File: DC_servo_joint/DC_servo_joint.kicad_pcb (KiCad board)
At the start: 2 copper layers, 58.5 x 50 mm, 52 parts, among them U1 AS5600, U2 ESP32-C3-WROOM-02, U3 SP3485EN, U5 TPS563200

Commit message: Add personal Mark to the silkscreen
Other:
- board text added: "Ca(OH)2"
- board text added: "LimeRobotLab"
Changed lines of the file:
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@@
 		)
 		(property "Value" "ESP32-C3-WROOM-02"
-			(at 0 -7.975 270)
+			(at -0.55 4.225 270)
 			(layer "B.SilkS")
 			(effects
@@
 		)
 	)
+	(gr_text "Ca(OH)2"
+		(at 137.125 83.625 270)
+		(layer "B.SilkS")
+		(effects
+			(font
+				(size 2.5 2.5)
+				(thickness 0.35)
+				(italic yes)
+			)
+			(justify left bottom mirror)
+		)
+	)
 	(gr_text "GND"
 		(at 134.375 93.95 -0)
@@
 			)
 			(justify left bottom mirror)
+		)
+	)
+	(gr_text "LimeRobotLab"
+		(at 133.875 83.225 270)
+		(layer "B.SilkS")
+		(effects
+			(font
+				(size 1.5 1.5)
+				(thickness 0.2)
+				(italic yes)
+			)
+			(justify left bottom mirror)

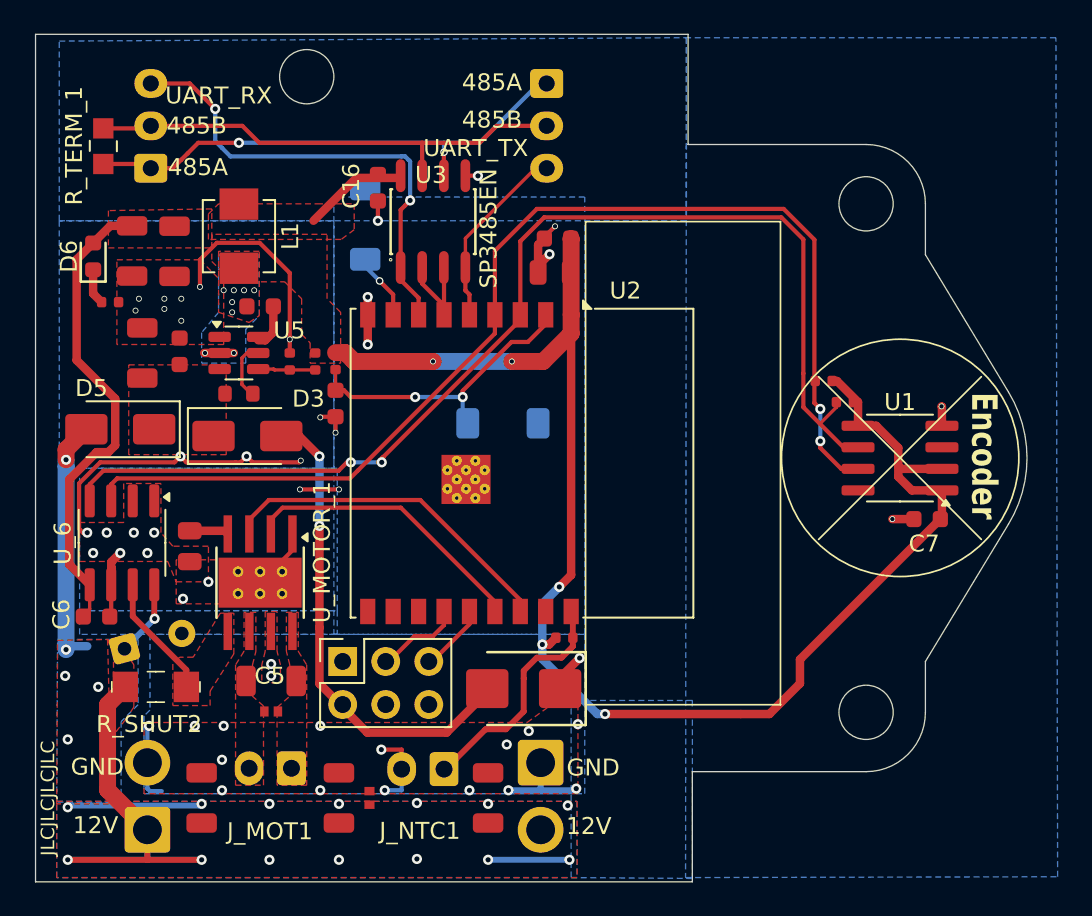
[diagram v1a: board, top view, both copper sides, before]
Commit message: Fixed the via size issue. Replace the INA219 with proper part
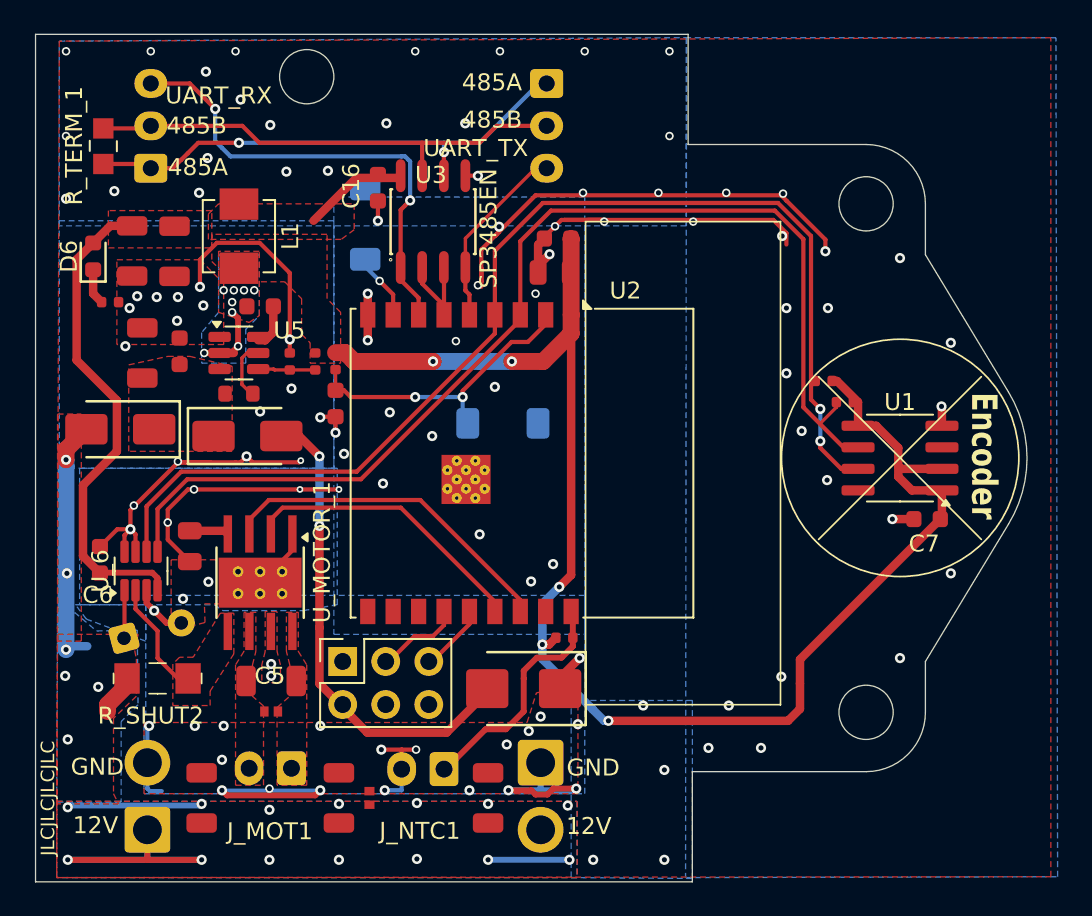
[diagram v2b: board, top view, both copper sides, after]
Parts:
- D3, D5: footprint Diode_SMD:D_SMA -> PCM_JLCPCB:D_SMA
- U_6: footprint Package_SO:SOIC-8_3.9x4.9mm_P1.27mm -> Package_TO_SOT_SMD:SOT-23-8
- moved C6 3.36 mm to (102.8, 81.0), turned to 90 degrees
- moved U_6 2.01 mm to (105.2, 81.7), turned to 90 degrees
- moved C15 0.62 mm to (104.2, 85.6)
- moved R_SHUT2 0.51 mm to (106.2, 88.0)
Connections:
- U_6 pad 1: GND -> +12V
- U_6 pad 2: GND -> /V_motor
- U_6 pad 3: /SDA -> GND
- U_6 pad 4: /SCL -> +3.3V
- U_6 pad 5: +3.3V -> /SCL
- U_6 pad 6: GND -> /SDA
- U_6 pad 7: /V_motor -> GND
- U_6 pad 8: +12V -> GND
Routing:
- net GND: track 70.3 -> 144.9 mm, vias 50 -> 111
- net +12V: track 61.3 -> 51.6 mm
- net /TPS_SW: track 1.75 -> 5.15 mm
- net /SCL: track 68.9 -> 66.8 mm, vias 2 -> 0
- net +3.3V: track 122.6 -> 124.5 mm
- net /pwm2_io3: track 17.2 -> 15.8 mm
- net /V_motor: track 7.34 -> 6.24 mm
- net /pwm1_io2: track 20.4 -> 19.6 mm

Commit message: Updated the proper value for INA219AxD and did part selection on JLC plugin
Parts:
- U_6: value INA219BxD -> INA219AxDCN
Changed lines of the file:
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@@
 			)
 		)
-		(property "Value" "INA219BxD"
+		(property "Value" "INA219AxDCN"
 			(at 0 2.4 90)
 			(layer "F.Fab")
@@
 			)
 		)
+		(property "LCSC" "C87469"
+			(at 0 0 0)
+			(layer "F.SilkS")
+			(hide yes)
+			(effects
+				(font
+					(size 1.27 1.27)
+					(thickness 0.15)
+				)
+			)
+		)
 		(property ki_fp_filters "SOT?23*")
 		(sheetname "/")
@@
 			(hide yes)
 			(effects
+				(font
+					(size 1.27 1.27)
+					(thickness 0.15)
+				)
+			)
+		)
+		(property "LCSC" "C97253"
+			(at 0 0 0)
+			(layer "F.SilkS")
+			(hide yes)
+			(effects

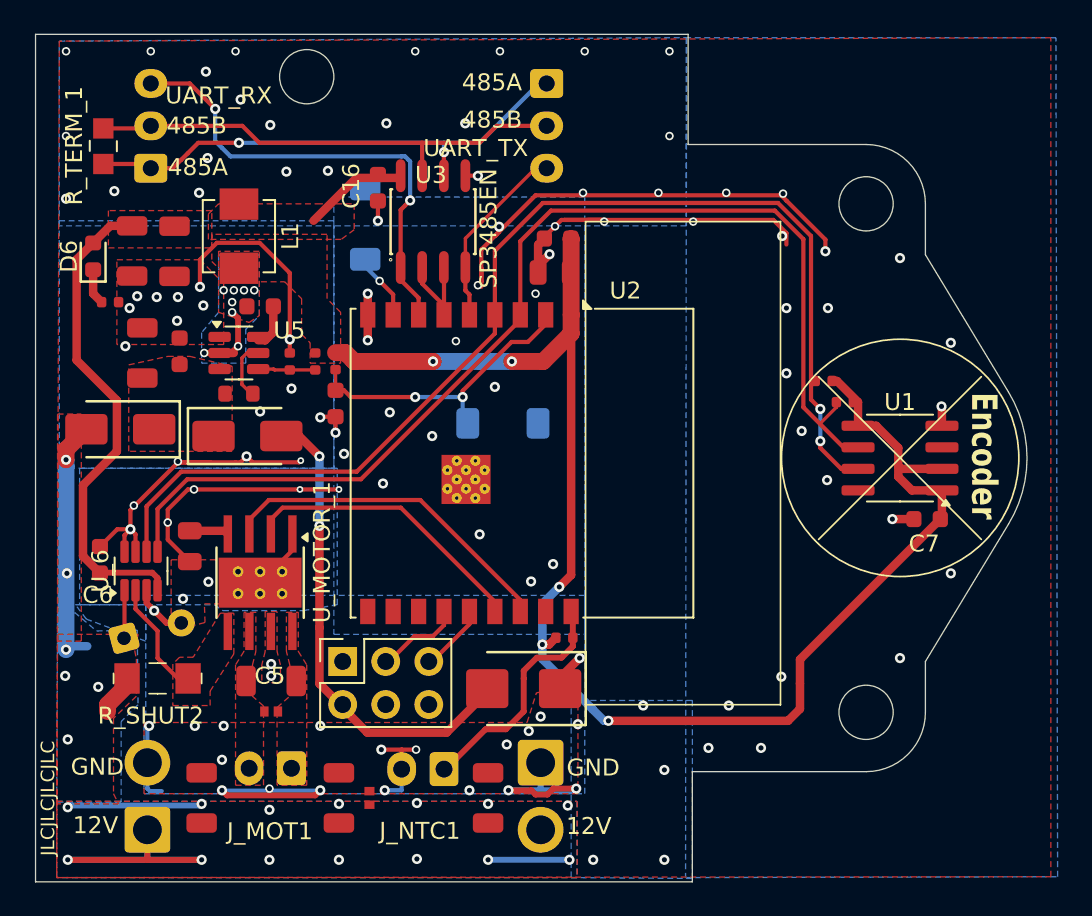
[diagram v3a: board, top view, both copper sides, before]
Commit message: Generated first trial of production file. Also added 2 rotations to parts.
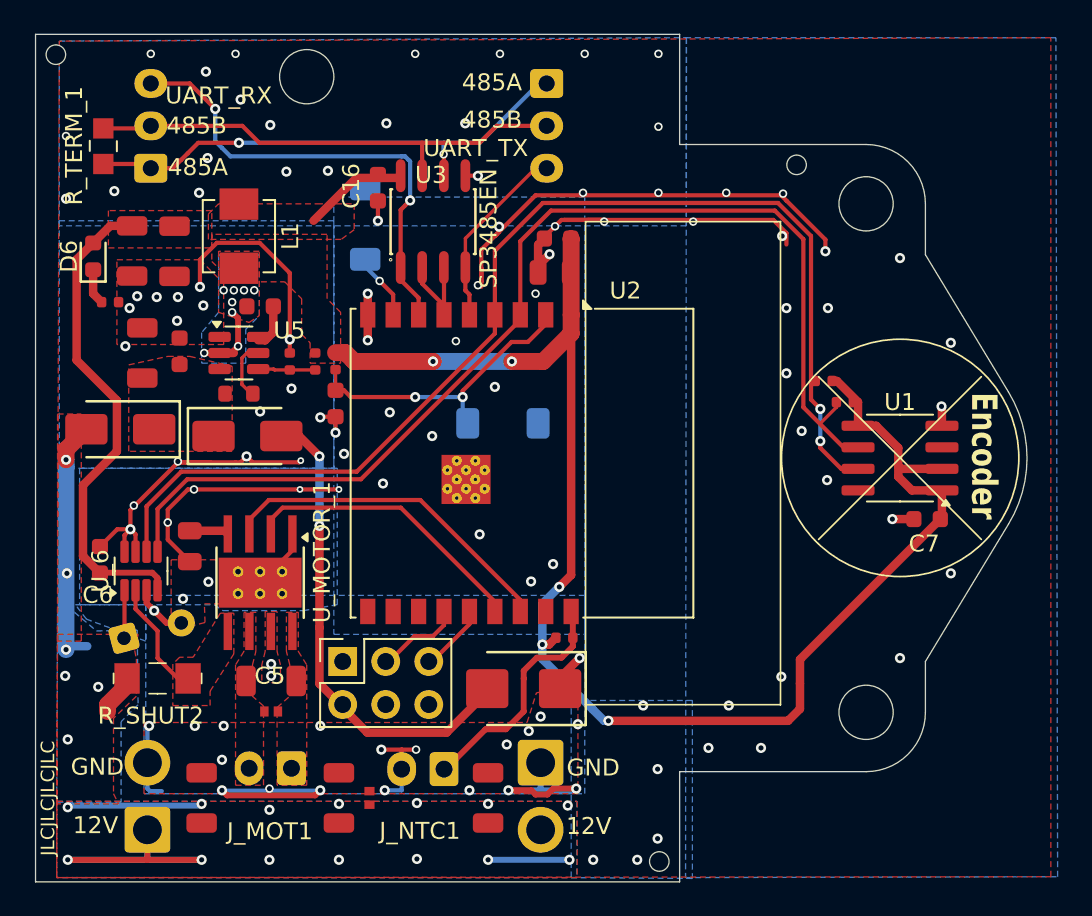
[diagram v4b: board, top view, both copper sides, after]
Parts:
- added H4: ~, PCM_JLCPCB:Hole_Tooling_JLCPCB, F.Cu at (143.9, 57.7)
- added H5: ~, PCM_JLCPCB:Hole_Tooling_JLCPCB, F.Cu at (100.2, 51.2)
- added H6: ~, PCM_JLCPCB:Hole_Tooling_JLCPCB, F.Cu at (135.8, 98.8)
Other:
- outline, holes or cut-outs redrawn

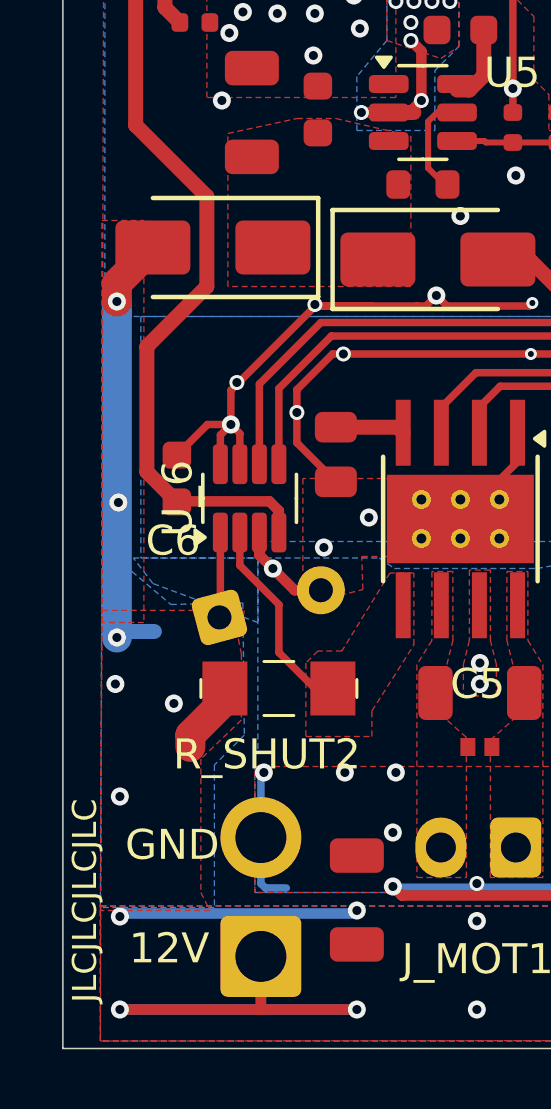
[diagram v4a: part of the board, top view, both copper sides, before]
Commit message: Add silkscreen in for usb header, Re generated production file
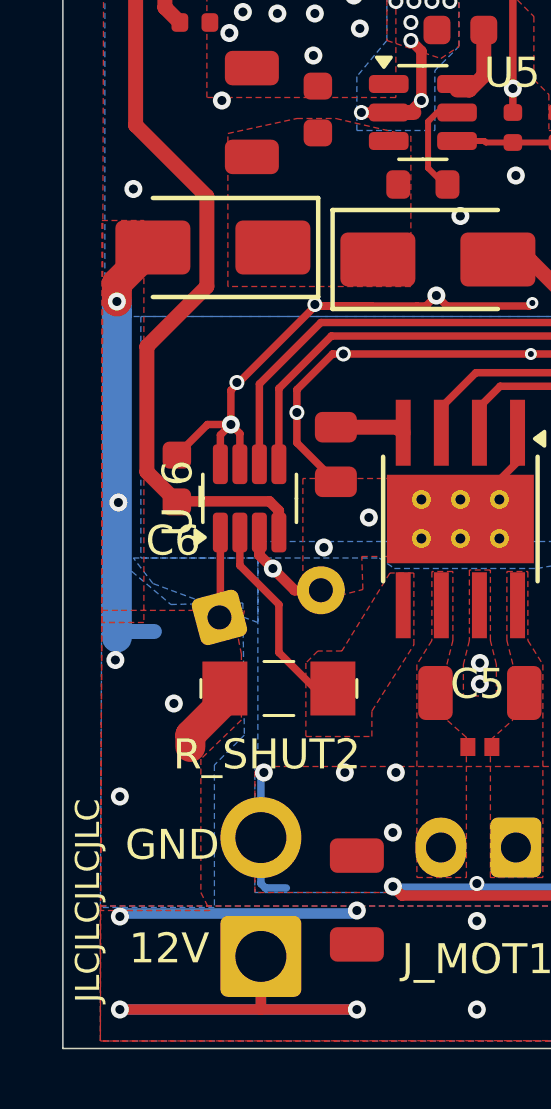
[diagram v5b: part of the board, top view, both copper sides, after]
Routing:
- net GND: vias 111 -> 112
- net +12V: vias 20 -> 19
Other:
- board text added: "5V"
- board text added: "D+"
- board text added: "D-"
- board text added: "DC Servo Joint v0.9"
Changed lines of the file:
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@@
 		(tags "DFN1006-2L-RD footprint C22395516")
 		(property "Reference" "D4"
-			(at 0.05 0.2 0)
+			(at 0.175 -0.075 0)
 			(layer "B.SilkS")
 			(effects
@@
 		)
 		(property "Value" "ESP32-C3-WROOM-02"
-			(at -0.55 4.225 270)
+			(at -0.2 3.05 270)
 			(layer "B.SilkS")
 			(effects
@@
 			)
 		)
+		(property "LCSC" "C2934560"
+			(at 0 0 270)
+			(unlocked yes)
+			(layer "F.Fab")
+			(hide yes)
+			(effects
+				(font
+					(size 1 1)
+					(thickness 0.15)
+				)
+			)
+		)
 		(property ki_fp_filters "ESP32?C3*WROOM?02*")
 		(sheetname "/")
@@
 		(tags "Through hole socket strip THT 2x03 2.54mm double row")
 		(property "Reference" "J_USB1"
-			(at 2.3 3.53 0)
+			(at 2.3 -0.07 0)
 			(layer "B.SilkS")
 			(effects
@@
 			)
 		)
+		(property "LCSC" "C7467249"
+			(at 0 0 180)
+			(unlocked yes)
+			(layer "F.Fab")
+			(hide yes)
+			(effects
+				(font
+					(size 1 1)
+					(thickness 0.15)
+				)
+			)
+		)
 		(property ki_fp_filters "R_*")
 		(sheetname "/")
@@
 			)
 		)
+		(property "LCSC" "C844973"
+			(at 0 0 270)
+			(unlocked yes)
+			(layer "F.Fab")
+			(hide yes)
+			(effects
+				(font
+					(size 1 1)
+					(thickness 0.15)
+				)
+			)
+		)
 		(property ki_fp_filters "Choke_* *Coil* Inductor_* L_*")
 		(sheetname "/")
@@
 	)
 	(gr_text "JLCJLCJLCJLC"
-		(at 100.2 98.475 90)
+		(at 100.3 98.475 90)
 		(layer "F.SilkS")
 		(effects
@@
 		)
 	)
+	(gr_text "5V"
+		(at 116.325 89.725 0)
+		(layer "B.SilkS")
+		(effects
+			(font
+				(size 1 1)
+				(thickness 0.1)
+			)
+			(justify left bottom mirror)
+		)
+	)
 	(gr_text "Ca(OH)2"
 		(at 137.125 83.625 270)
@@
 		)
 	)
+	(gr_text "D-"
+		(at 120.95 86.25 0)
+		(layer "B.SilkS")
+		(effects
+			(font
+				(size 1 1)
+				(thickness 0.1)
+			)
+			(justify left bottom mirror)
+		)
+	)
 	(gr_text "GND"
 		(at 134.375 93.95 -0)
@@
 		)
 	)
+	(gr_text "DC Servo Joint v0.9"
+		(at 131.75 83.075 270)
+		(layer "B.SilkS")
+		(effects
+			(font
+				(size 1 1)
+				(thickness 0.1)
+			)
+			(justify left bottom mirror)
+		)
+	)
 	(gr_text "12V"
 		(at 103.1 97.25 -0)
@@
 		)
 	)
+	(gr_text "GND"
+		(at 125.4 89.025 0)
+		(layer "B.SilkS")
+		(effects
+			(font
+				(size 1 1)
+				(thickness 0.1)
+			)
+			(justify left bottom mirror)
+		)
+	)
 	(gr_text "485A"
 		(at 111.85 58.475 0)
@@
 		)
 	)
+	(gr_text "D+"
+		(at 123.625 86.15 0)
+		(layer "B.SilkS")
+		(effects
+			(font
+				(size 1 1)
+				(thickness 0.1)
+			)
+			(justify left bottom mirror)
+		)
+	)
 	(gr_text "Encoder"
 		(at 155.825 71.125 -270)
@@
 	)
 	(via
+		(at 101.35 71.35)
+		(size 0.6)
+		(drill 0.3)
+		(layers "F.Cu" "B.Cu")
+		(net 3)
+	)
+	(via
 		(at 124.35 55.25)
 		(size 0.6)
@@
 	)
 	(via
-		(at 100.75 87.85)
+		(at 100.75 87.05)
 		(size 0.6)
 		(drill 0.3)
@@
 		(size 0.6)
 		(drill 0.3)
-		(layers "F.Cu" "B.Cu")
-		(net 4)
-	)
-	(via
-		(at 100.8 86.3)
-		(size 0.6)
-		(drill 0.3)

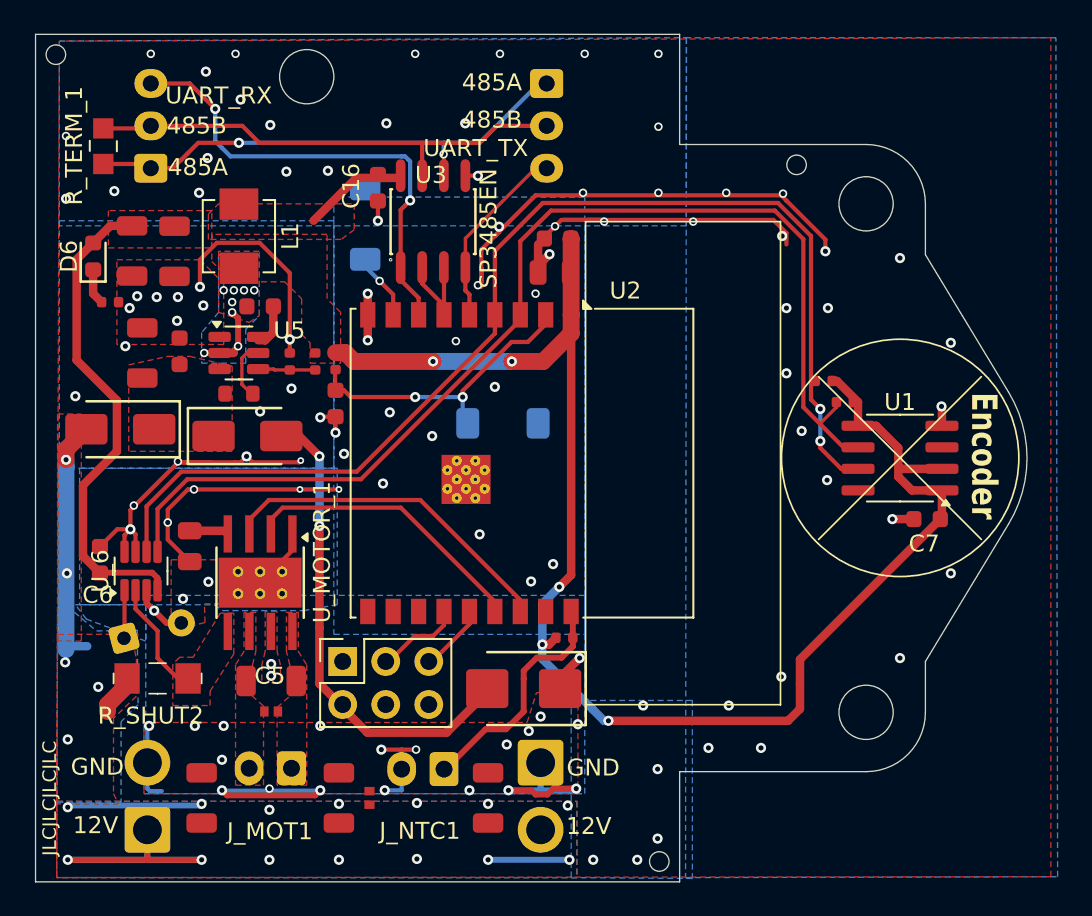
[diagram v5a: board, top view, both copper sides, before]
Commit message: Redo details caused by ambiguity,Redirect GPIO2
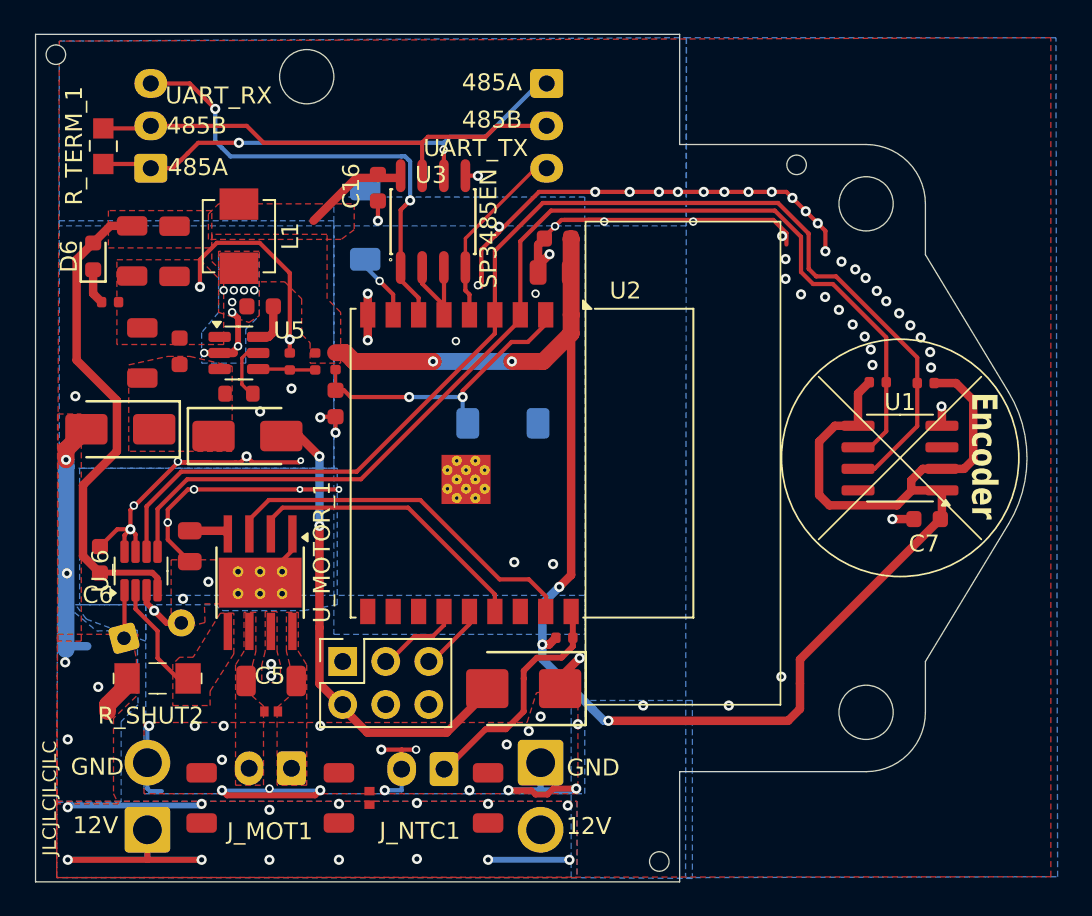
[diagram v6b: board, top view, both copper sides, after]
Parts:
- moved R_i2c2 6.02 mm to (151.5, 70.6)
- moved R_i2c1 2.27 mm to (148.7, 70.5), turned to 0 degrees
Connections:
- U2 pad 16: /pwm1_io2 -> unconnected-(U2-IO2-Pad16)
- U2 pad 17: unconnected-(U2-IO1-Pad17) -> /pwm1_io2
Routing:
- net +3.3V: track 124.5 -> 138.4 mm
- net /SDA: track 68.2 -> 71.8 mm, vias 2 -> 0
- net /pwm1_io2: track 19.6 -> 21.2 mm
- net /SCL: track 66.8 -> 68.0 mm
- net GND: track 144.9 -> 145.3 mm, vias 112 -> 91
